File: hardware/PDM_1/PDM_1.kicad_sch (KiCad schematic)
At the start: 6 parts, among them U1 STM32G0C1KCTxN

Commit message: Porządki w folderze
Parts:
- added J1: FTSH-107-01-L-DV-K-A, FTSH-107-01-L-DV-K-A:FTSH-107-XX-YYY-DV-K-A, symbol ftsh-107-01-l-dv-k-a:FTSH-107-01-L-DV-K-A
- added R1: 100k, Resistor_SMD:R_0603_1608Metric, symbol Device:R_Small
- FB1: footprint (none) -> Inductor_SMD:L_0603_1608Metric
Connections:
- net +3.3V: now also J1.3 (Pin_3), R1.2
- net CAN_RXD: now also U1.22 (PA11/PA9); no longer U1.26 (PD0)
- net CAN_TXD: now also U1.23 (PA12/PA10); no longer U1.27 (PD1)
- net GND: now also J1.11 (Pin_11), J1.5 (Pin_5), J1.7 (Pin_7)
- net STM_VCC: now reaches C1.1, C2.1, C3.1, C4.1, FB1.2, U1.20 (VDDIO2), U1.4 (VDD)
- net FUSE4_IS: now reaches U1.10 (PA3)
- net SPI1_NSS: now reaches U1.11 (PA4)
- net SPI1_SCK: now reaches U1.12 (PA5)
- net SPI1_MISO: now reaches U1.13 (PA6)
- net SPI1_MOSI: now reaches U1.14 (PA7)
- net LHI_3: now reaches U1.15 (PB0)
- net LHI_4: now reaches U1.16 (PB1)
- net LED3: now reaches U1.17 (PB15)
- net LED2: now reaches U1.18 (PA8)
- net LED1: now reaches U1.19 (PA9/UCPD1_DBCC1)
- net SWDIO: now reaches U1.24 (PA13)
- net SWDIO: now also J1.4 (Pin_4)
- net SWCLK: now reaches U1.25 (PA14)
- net SWCLK: now also J1.6 (Pin_6)
- net LHI_1: now reaches U1.28 (PD2)
- net LHI_2: now reaches U1.29 (PD3)
- net USART1_TX: now reaches U1.30 (PB6)
- net USART1_TX: now also J1.14 (Pin_14)
- net USART1_RX: now reaches U1.31 (PB7)
- net USART1_RX: now also J1.13 (Pin_13)
- net NRST: now reaches U1.6 (PF2)
- net NRST: now also J1.12 (Pin_12), R1.1
- net FUSE1_IS: now reaches U1.7 (PA0)
- net FUSE2_IS: now reaches U1.8 (PA1)
- net FUSE3_IS: now reaches U1.9 (PA2)
- no-connect marks 0 -> 12
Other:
- removed sheet power distribution
- added sheet LED (LED.kicad_sch)
- added sheet connectors (connectors.kicad_sch)
- sheet battery connection ports: added CSN, IS_1, IS_2, IS_3, IS_4, LHI_1, LHI_2, LHI_3, LHI_4, MISO, MOSI, SCLK; removed none
- note added: "?"
- note added: "can_rxd"
- note added: "can_txd ???"
- note added: "złącza"
- moved on the sheet: C1, C2, C3, C4, FB1, U1

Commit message: Poprawki6
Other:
- note removed: "can_rxd"
- note removed: "can_txd ???"
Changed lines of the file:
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@@
     (fill (type none))
-  )
-  (text "can_txd\n???" (at 203.2 55.88 0)
-    (effects (font (size 1.27 1.27)) (justify left bottom))
   )
   (text "?" (at 176.53 31.75 0)
     (effects (font (size 1.27 1.27)) (justify left bottom))
   )
-  (text "can_rxd" (at 203.2 52.07 0)
-    (effects (font (size 1.27 1.27)) (justify left bottom))
-  )

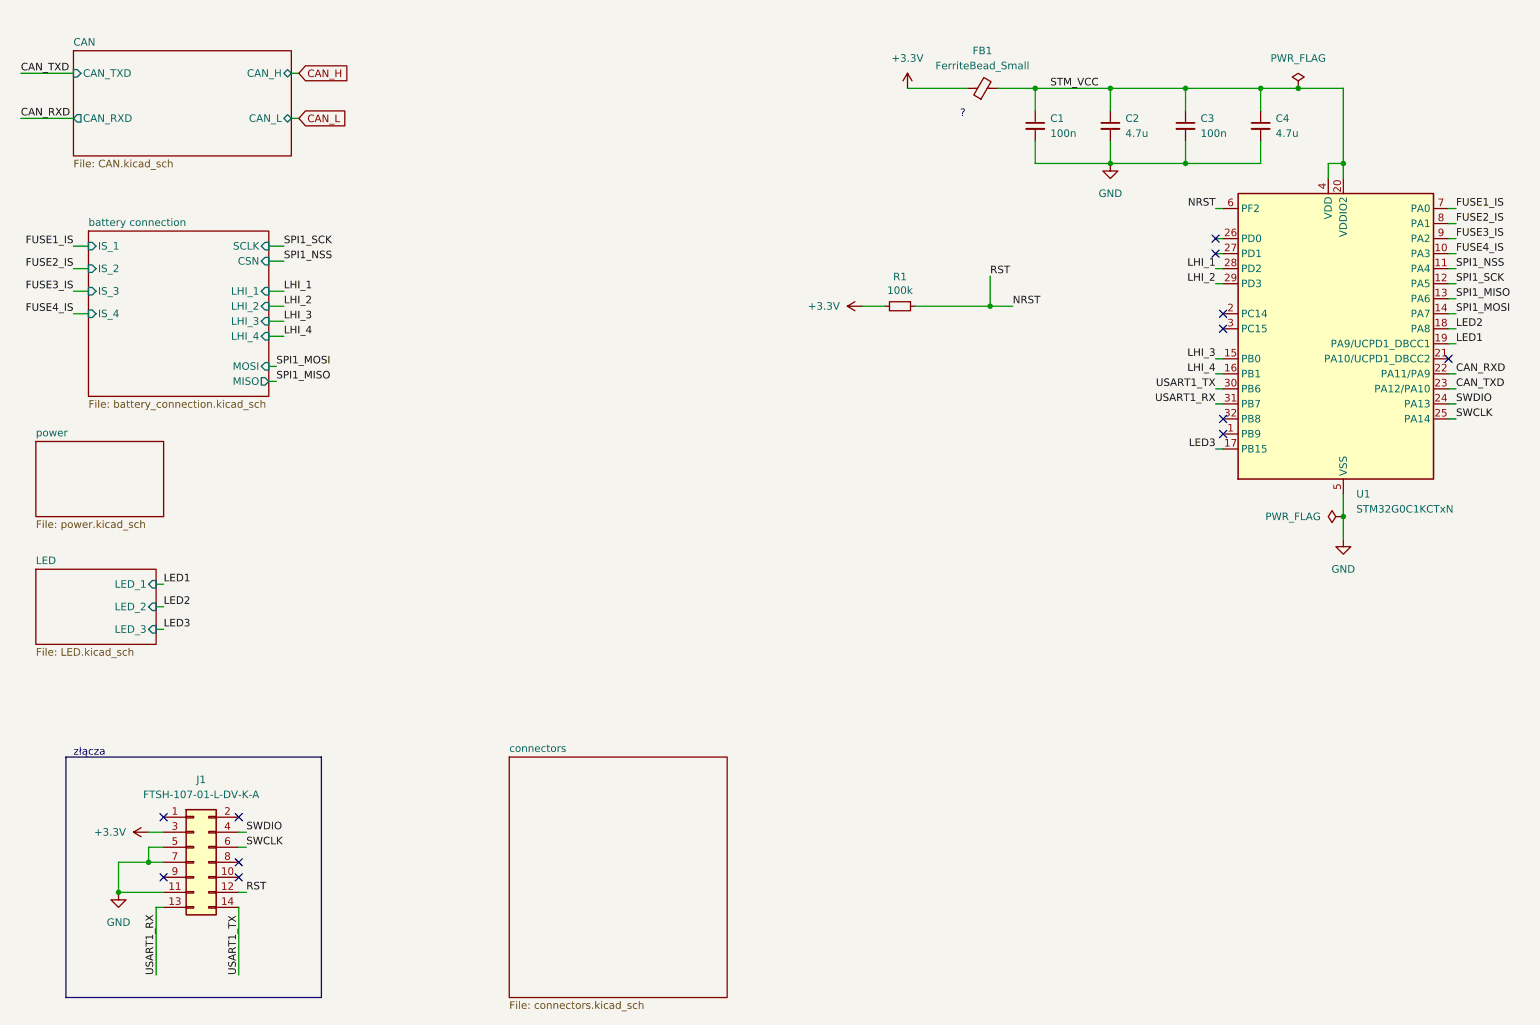
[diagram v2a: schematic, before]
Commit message: Transfer from PDM to simple FuseBox
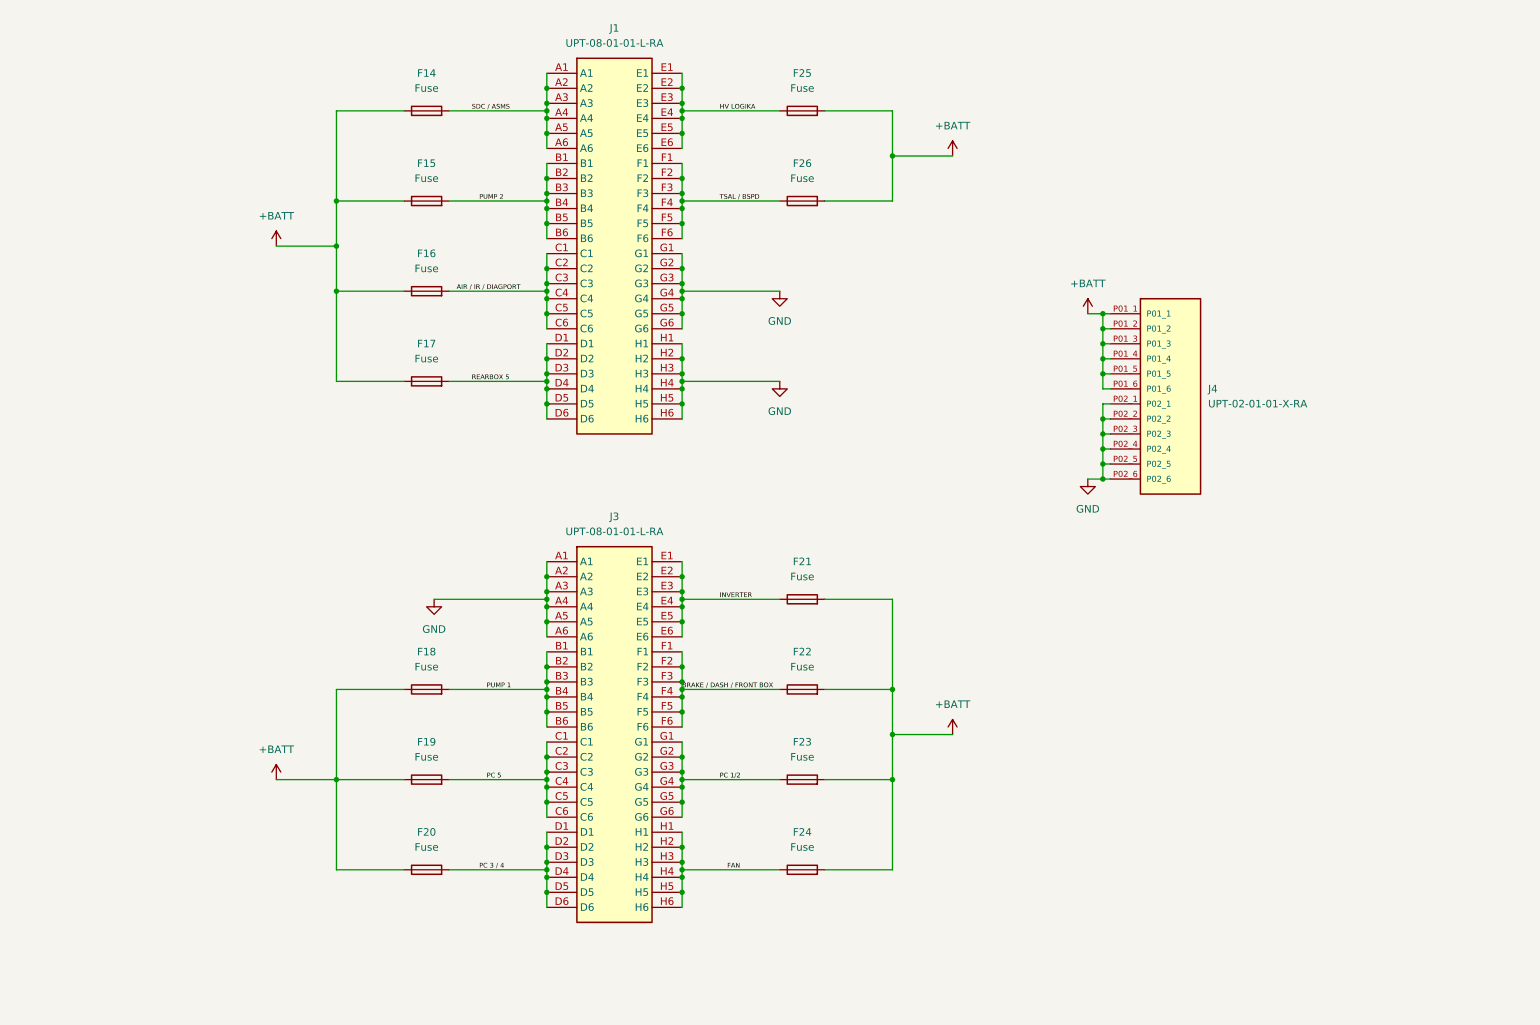
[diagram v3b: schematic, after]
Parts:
- removed C1, C3: 100n, Inductor_SMD:L_0603_1608Metric, symbol Device:C_Small
- removed C2, C4: 4.7u, Inductor_SMD:L_0603_1608Metric, symbol Device:C_Small
- removed FB1: FerriteBead_Small, Inductor_SMD:L_0603_1608Metric, symbol Device:FerriteBead_Small
- removed J1: FTSH-107-01-L-DV-K-A, FTSH-107-01-L-DV-K-A:FTSH-107-XX-YYY-DV-K-A, symbol ftsh-107-01-l-dv-k-a:FTSH-107-01-L-DV-K-A
- removed R1: 100k, Resistor_SMD:R_0603_1608Metric, symbol Device:R_Small
- removed U1: STM32G0C1KCTxN, Package_QFP:LQFP-32_7x7mm_P0.8mm, symbol MCU_ST_STM32G0:STM32G0C1KCTxN
- added F14, F15, F16, F17, F18, F19, F20, F21, F22, F23, F24, F25, F26: Fuse, LIB_3568:3568, symbol Device:Fuse
- added J1, J3: UPT-08-01-01-L-RA, UPT080101LRA, symbol 8pin_good:UPT-08-01-01-L-RA
- added J4: UPT-02-01-01-X-RA, 2pin:SAMTEC_UPT-02-01-01-X-RA, symbol 2pin:UPT-02-01-01-X-RA
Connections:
- net GND: now also J1.G1, J1.G2, J1.G3, J1.G4, J1.G5, J1.G6, J1.H1, J1.H2, J1.H3, J1.H4, J1.H5, J1.H6, J3.A1, J3.A2, J3.A3, J3.A4, J3.A5, J3.A6, J4.P02_1, J4.P02_2, J4.P02_3, J4.P02_4, J4.P02_5, J4.P02_6
- new net +BATT: F14.1, F15.1, F16.1, F17.1, F18.1, F19.1, F20.1, F21.2, F22.2, F23.2, F24.2, F25.2, F26.2, J4.P01_1, J4.P01_2, J4.P01_3, J4.P01_4, J4.P01_5, J4.P01_6
- new net AIR / IR / DIAGPORT: F16.2, J1.C1, J1.C2, J1.C3, J1.C4, J1.C5, J1.C6
- new net BRAKE / DASH / FRONT BOX: F22.1, J3.F1, J3.F2, J3.F3, J3.F4, J3.F5, J3.F6
- new net FAN: F24.1, J3.H1, J3.H2, J3.H3, J3.H4, J3.H5, J3.H6
- new net HV LOGIKA: F25.1, J1.E1, J1.E2, J1.E3, J1.E4, J1.E5, J1.E6
- new net INVERTER: F21.1, J3.E1, J3.E2, J3.E3, J3.E4, J3.E5, J3.E6
- new net PC 1/2: F23.1, J3.G1, J3.G2, J3.G3, J3.G4, J3.G5, J3.G6
- new net PC 3 / 4: F20.2, J3.D1, J3.D2, J3.D3, J3.D4, J3.D5, J3.D6
- new net PC 5: F19.2, J3.C1, J3.C2, J3.C3, J3.C4, J3.C5, J3.C6
- new net PUMP 1: F18.2, J3.B1, J3.B2, J3.B3, J3.B4, J3.B5, J3.B6
- new net PUMP 2: F15.2, J1.B1, J1.B2, J1.B3, J1.B4, J1.B5, J1.B6
- new net REARBOX 5: F17.2, J1.D1, J1.D2, J1.D3, J1.D4, J1.D5, J1.D6
- new net SDC / ASMS: F14.2, J1.A1, J1.A2, J1.A3, J1.A4, J1.A5, J1.A6
- new net TSAL / BSPD: F26.1, J1.F1, J1.F2, J1.F3, J1.F4, J1.F5, J1.F6
- no-connect marks 12 -> 0
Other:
- removed sheet CAN
- removed sheet LED
- removed sheet battery connection
- removed sheet connectors
- removed sheet power
- note removed: "?"
- note removed: "złącza"
